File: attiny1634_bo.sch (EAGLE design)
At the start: 11 parts, among them J1 AVR_SPI_PRG_6NS, Y1 16MHz

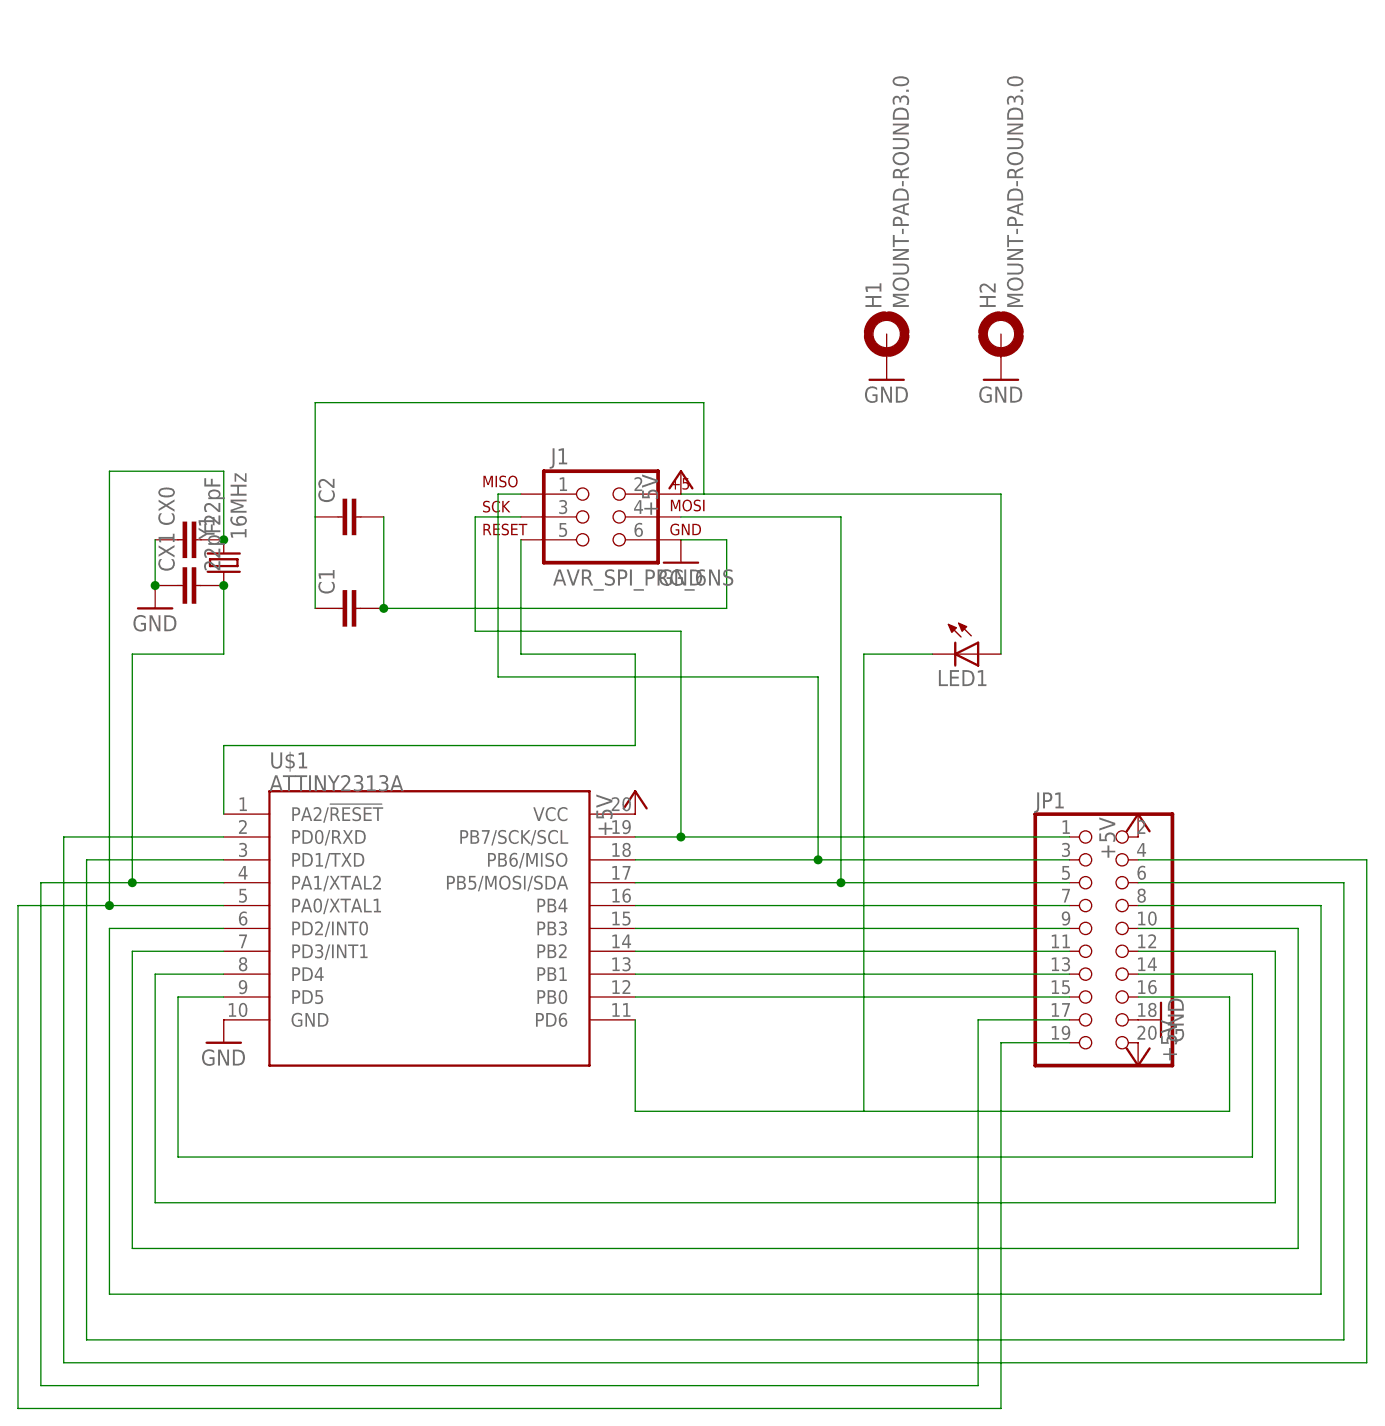
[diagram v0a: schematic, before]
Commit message: use the new part and remove old wires from schematic
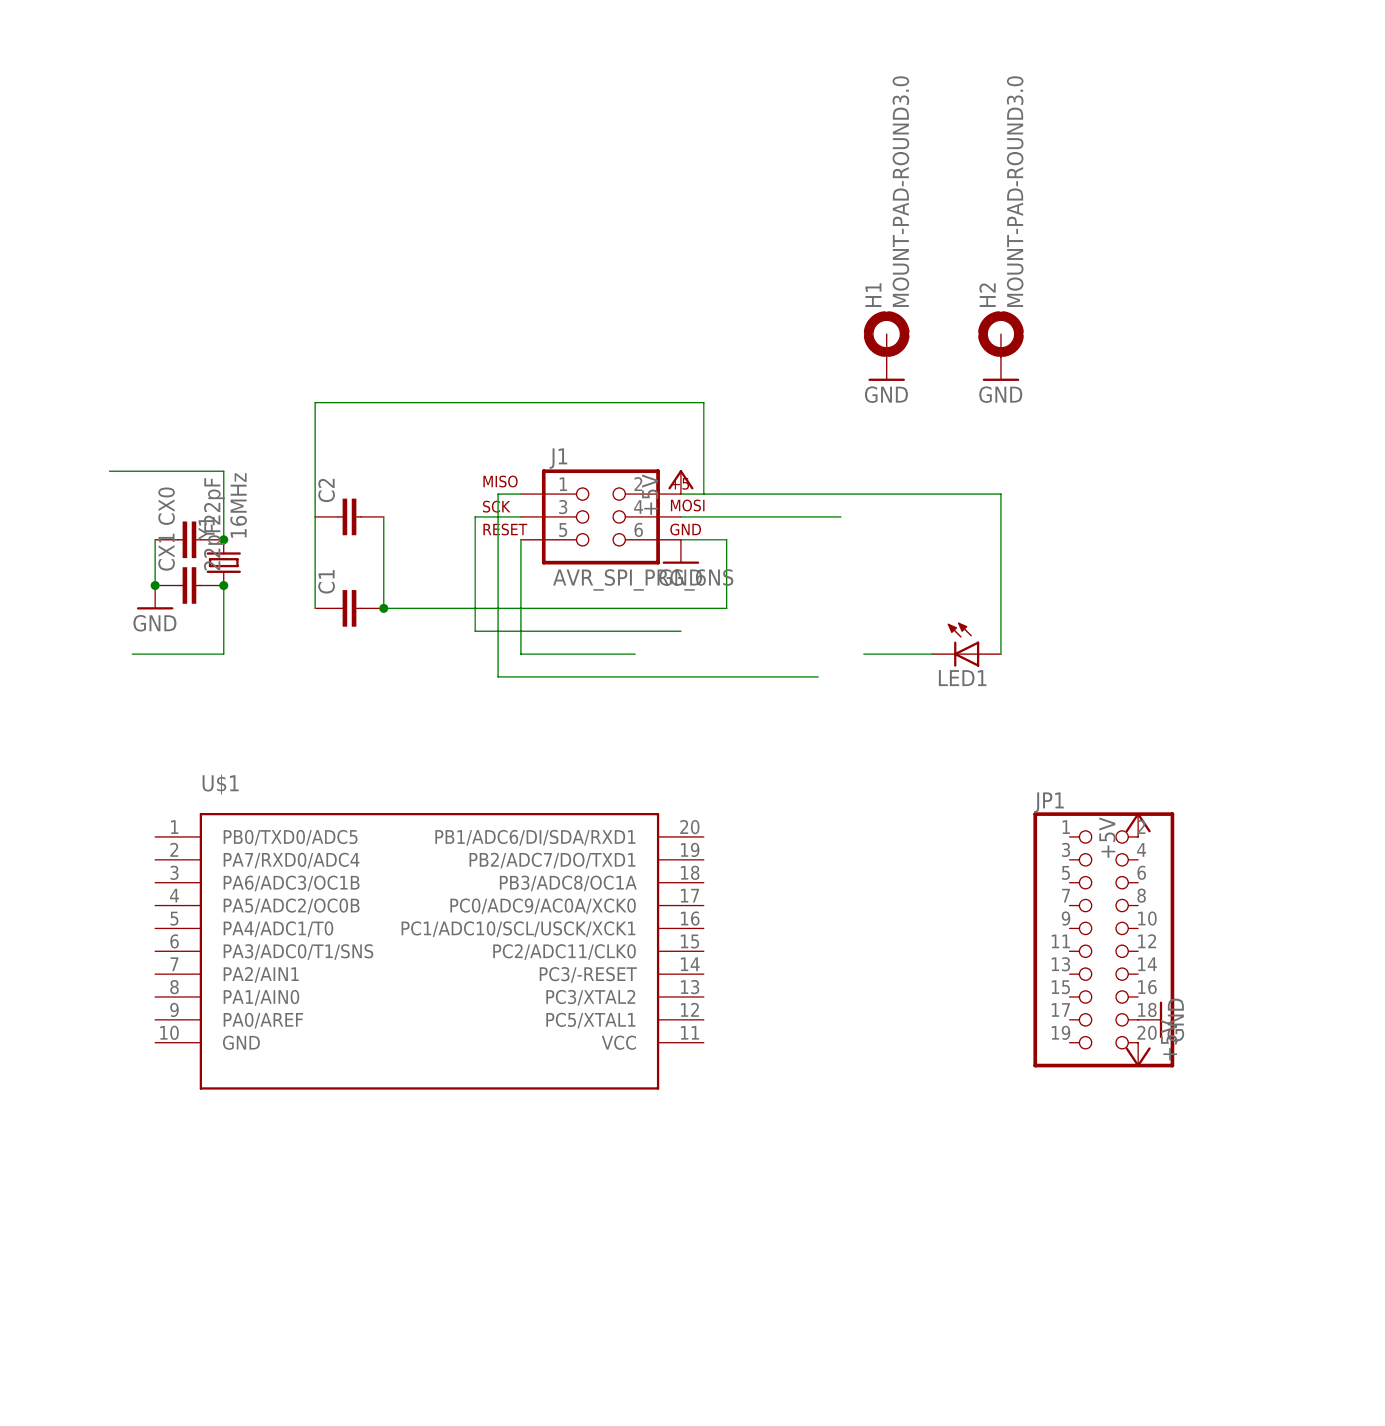
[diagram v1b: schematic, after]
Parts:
- U$1: value ATTINY2313A -> ATTINY1634; device SparkFun-DigitalIC:ATTINY2313A -> attiny1634:ATTINY1634
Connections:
- removed net PA0/XTAL1: CX0.2, JP1.19, U$1.PA0/XTAL1, Y1.2
- removed net PA1/XTAL2: CX1.2, JP1.17, U$1.PA1/XTAL2, Y1.1
- removed net PA2/RESET-: J1.5, U$1.PA2/!RESET
- removed net PB0: JP1.15, U$1.PB0
- removed net PB1: JP1.13, U$1.PB1
- removed net PB2: JP1.11, U$1.PB2
- removed net PB3: JP1.9, U$1.PB3
- removed net PB4: JP1.7, U$1.PB4
- removed net PB5/MOSI: J1.4, JP1.5, U$1.PB5/MOSI/SDA
- removed net PB7/SCL: J1.3, JP1.1, U$1.PB7/SCK/SCL
- removed net PD0/RDX: JP1.4, U$1.PD0/RXD
- removed net PD1/TXD: JP1.6, U$1.PD1/TXD
- removed net PD2: JP1.8, U$1.PD2/INT0
- removed net PD3: JP1.10, U$1.PD3/INT1
- removed net PD4: JP1.12, U$1.PD4
- removed net PD5: JP1.14, U$1.PD5
- new net N$11: CX0.2, Y1.2
- new net N$3: J1.5
- new net N$4: J1.4
- new net N$7: J1.3
- new net N$9: CX1.2, Y1.1
- net +5V: no longer U$1.VCC
- net GND: no longer U$1.GND
- net PB6/MISO: no longer JP1.3, U$1.PB6/MISO
- net PD6: no longer JP1.16, U$1.PD6
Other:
- moved on the sheet: U$1

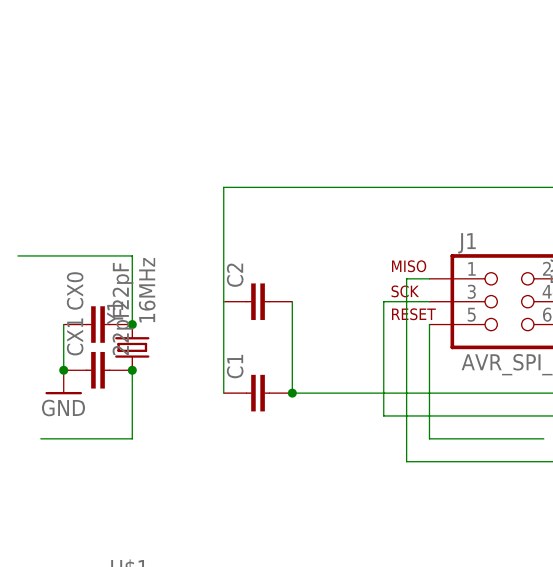
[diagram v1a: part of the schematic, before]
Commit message: 12MHz max speed for this part
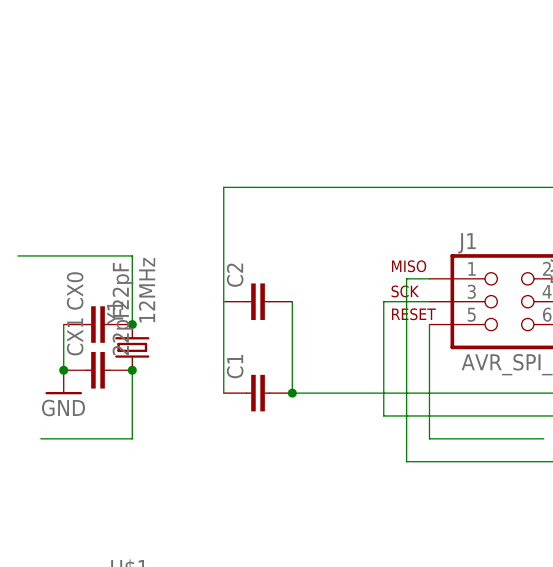
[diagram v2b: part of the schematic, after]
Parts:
- Y1: value 16MHz -> 12MHz
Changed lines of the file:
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@@
 <part name="CX1" library="rcl" deviceset="C-EU" device="C0603" value="22pF"/>
 <part name="GND4" library="supply1" deviceset="GND" device=""/>
-<part name="Y1" library="SparkFun-FreqCtrl" deviceset="CRYSTAL" device="5X3" value="16MHz"/>
+<part name="Y1" library="SparkFun-FreqCtrl" deviceset="CRYSTAL" device="5X3" value="12MHz"/>
 <part name="H1" library="holes" deviceset="MOUNT-PAD-ROUND" device="3.0"/>
 <part name="GND6" library="supply1" deviceset="GND" device=""/>

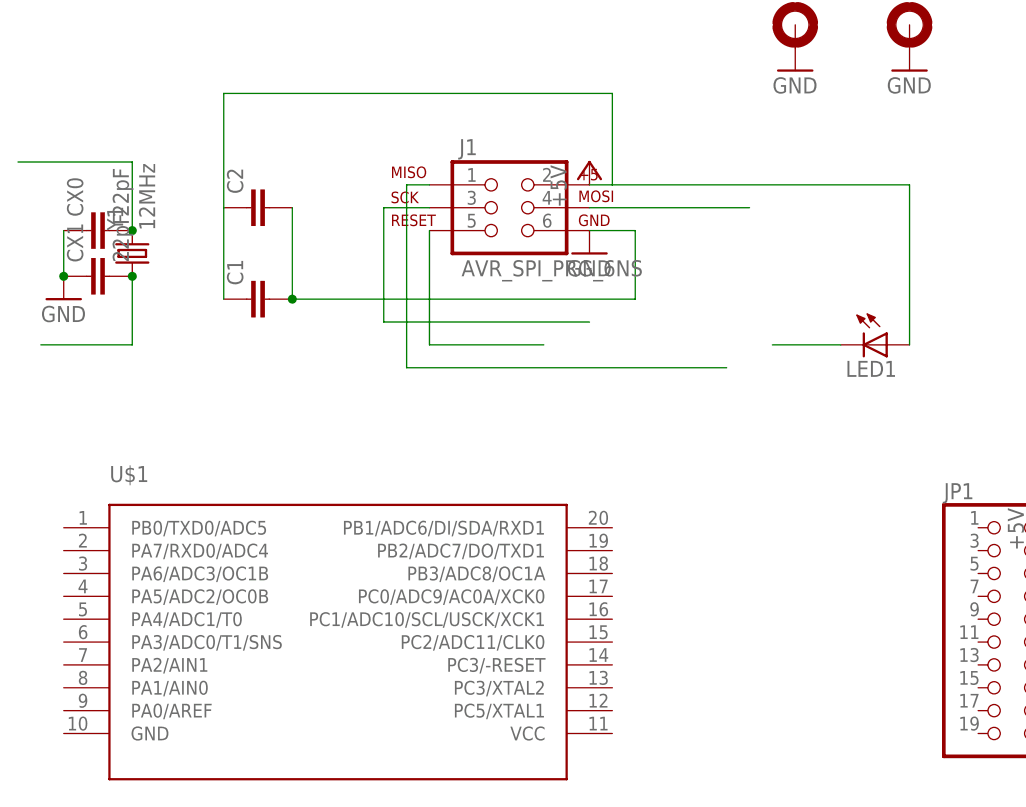
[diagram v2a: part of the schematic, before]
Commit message: minor fixes to the lib, connected programming signals and xtal
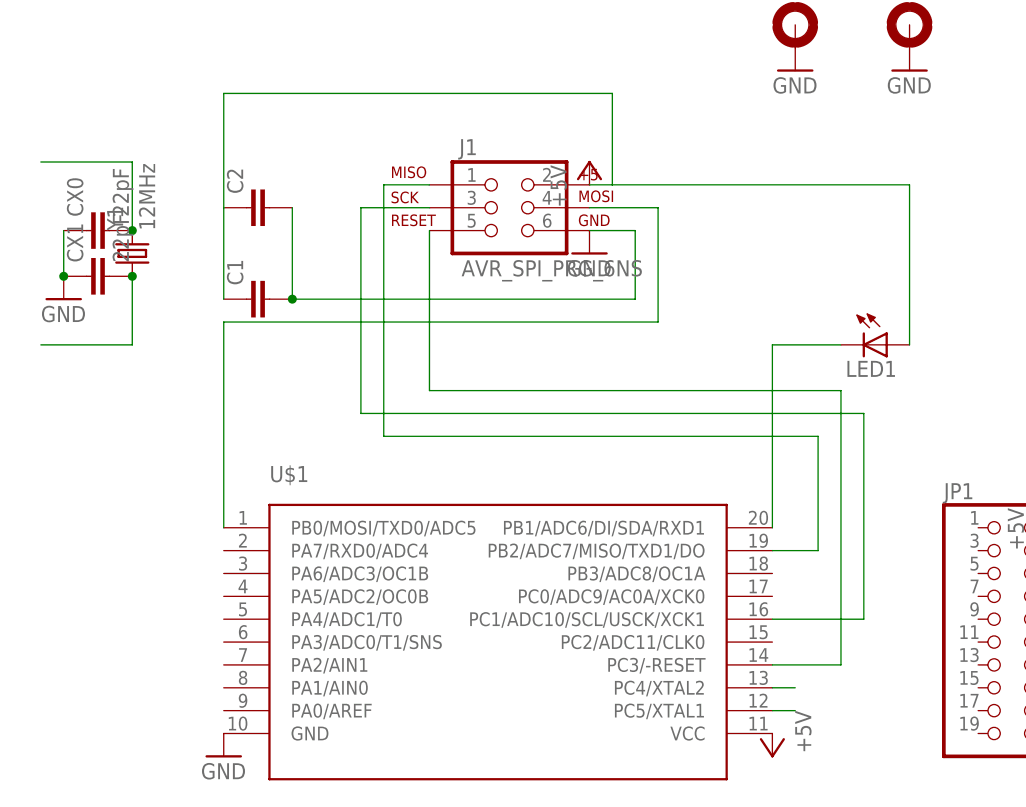
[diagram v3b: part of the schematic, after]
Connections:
- removed net N$11: CX0.2, Y1.2
- removed net N$3: J1.5
- removed net N$4: J1.4
- removed net N$7: J1.3
- removed net N$9: CX1.2, Y1.1
- removed net PB6/MISO: J1.1
- removed net PD6: LED1.C
- new net PB0/MOSI/TX0/ADC5: J1.4, U$1.PB0/MOSI/TXD0/ADC5
- new net PB1/ADC6: LED1.C, U$1.PB1/ADC6/DI/SDA/RXD1
- new net PB2/ADC7/TX1: J1.1, U$1.PB2/ADC7/MISO/TXD1/DO
- new net PC1/SCL/ADC10: J1.3, U$1.PC1/ADC10/SCL/USCK/XCK1
- new net PC3/-RESET: J1.5, U$1.PC3/-RESET
- new net PC4/XTAL2: CX0.2, U$1.PC4/XTAL2, Y1.2
- new net PC5/XTAL1: CX1.2, U$1.PC5/XTAL1, Y1.1
- net +5V: now also U$1.VCC
- net GND: now also U$1.GND
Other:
- moved on the sheet: U$1
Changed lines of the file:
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@@
 <part name="GND2" library="supply1" deviceset="GND" device=""/>
 <part name="U$1" library="attiny1634" deviceset="ATTINY1634" device=""/>
+<part name="P+1" library="supply1" deviceset="+5V" device=""/>
+<part name="GND1" library="supply1" deviceset="GND" device=""/>
 </parts>
 <sheets>
@@
 <instance part="P+3" gate="1" x="127" y="45.72" rot="R180"/>
 <instance part="GND2" gate="1" x="129.54" y="50.8" rot="R90"/>
-<instance part="U$1" gate="G$1" x="17.78" y="43.18"/>
+<instance part="U$1" gate="G$1" x="66.04" y="71.12"/>
+<instance part="P+1" gate="1" x="96.52" y="45.72" rot="R180"/>
+<instance part="GND1" gate="1" x="35.56" y="45.72"/>
 </instances>
 <busses>
@@
 <pinref part="GND2" gate="1" pin="GND"/>
 </segment>
+<segment>
+<pinref part="U$1" gate="G$1" pin="GND"/>
+<pinref part="GND1" gate="1" pin="GND"/>
+</segment>
 </net>
 <net name="+5V" class="1">
@@
 <pinref part="P+3" gate="1" pin="+5V"/>
 </segment>
-</net>
-<net name="PB6/MISO" class="0">
 <segment>
-<pinref part="J1" gate="G$1" pin="1"/>
-<wire x1="58.42" y1="109.22" x2="55.88" y2="109.22" width="0.1524" layer="91"/>
-<wire x1="55.88" y1="109.22" x2="55.88" y2="88.9" width="0.1524" layer="91"/>
-<wire x1="55.88" y1="88.9" x2="91.44" y2="88.9" width="0.1524" layer="91"/>
+<pinref part="U$1" gate="G$1" pin="VCC"/>
+<pinref part="P+1" gate="1" pin="+5V"/>
 </segment>
 </net>
-<net name="PD6" class="0">
+<net name="PB1/ADC6" class="0">
 <segment>
 <pinref part="LED1" gate="G$1" pin="C"/>
 <wire x1="96.52" y1="91.44" x2="104.14" y2="91.44" width="0.1524" layer="91"/>
+<pinref part="U$1" gate="G$1" pin="PB1/ADC6/DI/SDA/RXD1"/>
+<wire x1="96.52" y1="71.12" x2="96.52" y2="91.44" width="0.1524" layer="91"/>
 </segment>
 </net>
-<net name="N$3" class="0">
+<net name="PB0/MOSI/TX0/ADC5" class="0">
 <segment>
-<pinref part="J1" gate="G$1" pin="5"/>
-<wire x1="71.12" y1="91.44" x2="58.42" y2="91.44" width="0.1524" layer="91"/>
-<wire x1="58.42" y1="91.44" x2="58.42" y2="104.14" width="0.1524" layer="91"/>
+<pinref part="J1" gate="G$1" pin="4"/>
+<wire x1="76.2" y1="106.68" x2="83.82" y2="106.68" width="0.1524" layer="91"/>
+<wire x1="83.82" y1="106.68" x2="83.82" y2="93.98" width="0.1524" layer="91"/>
+<pinref part="U$1" gate="G$1" pin="PB0/MOSI/TXD0/ADC5"/>
+<wire x1="83.82" y1="93.98" x2="35.56" y2="93.98" width="0.1524" layer="91"/>
+<wire x1="35.56" y1="93.98" x2="35.56" y2="71.12" width="0.1524" layer="91"/>
 </segment>
 </net>
-<net name="N$4" class="0">
+<net name="PC1/SCL/ADC10" class="0">
 <segment>
-<pinref part="J1" gate="G$1" pin="4"/>
-<wire x1="93.98" y1="106.68" x2="76.2" y2="106.68" width="0.1524" layer="91"/>
+<pinref part="U$1" gate="G$1" pin="PC1/ADC10/SCL/USCK/XCK1"/>
+<wire x1="96.52" y1="60.96" x2="106.68" y2="60.96" width="0.1524" layer="91"/>
+<wire x1="106.68" y1="60.96" x2="106.68" y2="83.82" width="0.1524" layer="91"/>
+<wire x1="106.68" y1="83.82" x2="50.8" y2="83.82" width="0.1524" layer="91"/>
+<wire x1="50.8" y1="83.82" x2="50.8" y2="106.68" width="0.1524" layer="91"/>
+<pinref part="J1" gate="G$1" pin="3"/>
+<wire x1="50.8" y1="106.68" x2="58.42" y2="106.68" width="0.1524" layer="91"/>
 </segment>
 </net>
-<net name="N$7" class="0">
+<net name="PB2/ADC7/TX1" class="0">
 <segment>
-<pinref part="J1" gate="G$1" pin="3"/>
-<wire x1="58.42" y1="106.68" x2="53.34" y2="106.68" width="0.1524" layer="91"/>
-<wire x1="53.34" y1="106.68" x2="53.34" y2="93.98" width="0.1524" layer="91"/>
-<wire x1="53.34" y1="93.98" x2="76.2" y2="93.98" width="0.1524" layer="91"/>
+<pinref part="U$1" gate="G$1" pin="PB2/ADC7/MISO/TXD1/DO"/>
+<wire x1="96.52" y1="68.58" x2="101.6" y2="68.58" width="0.1524" layer="91"/>
+<wire x1="101.6" y1="68.58" x2="101.6" y2="81.28" width="0.1524" layer="91"/>
+<wire x1="101.6" y1="81.28" x2="53.34" y2="81.28" width="0.1524" layer="91"/>
+<wire x1="53.34" y1="81.28" x2="53.34" y2="109.22" width="0.1524" layer="91"/>
+<pinref part="J1" gate="G$1" pin="1"/>
+<wire x1="53.34" y1="109.22" x2="58.42" y2="109.22" width="0.1524" layer="91"/>
 </segment>
 </net>
-<net name="N$9" class="0">
+<net name="PC3/-RESET" class="0">
+<segment>
+<pinref part="U$1" gate="G$1" pin="PC3/-RESET"/>
+<wire x1="96.52" y1="55.88" x2="104.14" y2="55.88" width="0.1524" layer="91"/>
+<wire x1="104.14" y1="55.88" x2="104.14" y2="86.36" width="0.1524" layer="91"/>
+<pinref part="J1" gate="G$1" pin="5"/>
+<wire x1="104.14" y1="86.36" x2="58.42" y2="86.36" width="0.1524" layer="91"/>
+<wire x1="58.42" y1="86.36" x2="58.42" y2="104.14" width="0.1524" layer="91"/>
+</segment>
+</net>
+<net name="PC5/XTAL1" class="0">
+<segment>
+<pinref part="U$1" gate="G$1" pin="PC5/XTAL1"/>
+<wire x1="96.52" y1="50.8" x2="99.06" y2="50.8" width="0.1524" layer="91"/>
+</segment>
 <segment>
 <pinref part="CX1" gate="G$1" pin="2"/>
@@
 </segment>
 </net>
-<net name="N$11" class="0">
+<net name="PC4/XTAL2" class="0">
+<segment>
+<pinref part="U$1" gate="G$1" pin="PC4/XTAL2"/>
+<wire x1="96.52" y1="53.34" x2="99.06" y2="53.34" width="0.1524" layer="91"/>
+</segment>
 <segment>
 <pinref part="CX0" gate="G$1" pin="2"/>
@@
 <junction x="25.4" y="104.14"/>
 <wire x1="25.4" y1="104.14" x2="25.4" y2="111.76" width="0.1524" layer="91"/>
-<wire x1="25.4" y1="111.76" x2="12.7" y2="111.76" width="0.1524" layer="91"/>
+<wire x1="25.4" y1="111.76" x2="15.24" y2="111.76" width="0.1524" layer="91"/>
 </segment>
 </net>
